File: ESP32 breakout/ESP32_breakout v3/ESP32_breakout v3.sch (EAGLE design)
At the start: 54 parts, among them J3 SCHA4B0419, Q3 BSS84, U1 ESP-WROOM-32, U2 NCP-1117223-3, U3 MCP2221ATSSOP14

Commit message: Layout and 80% routing done
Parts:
- removed R13: 10k, dr-library:RESISTOR0603
- added JP7, JP8: JUMPER_2-WAY, dr-library:JUMPER_2-WAY
- added R3: 10k, dr-library:RESISTOR0603
- renumbered S1 to RST, S2 to BOOT
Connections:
- new net N$1: JP7.1, R9.1
- new net N$6: JP8.1, R3.1
- net +3V3: now also JP7.2, JP8.2; no longer R13.1, R9.1
- net CLK: no longer J3.CLK, R12.2
- net CMD: no longer J3.CMD, R11.2
- net IO12/T5: now also J3.DAT2, R9.2
- net IO13/T4: now also J3.DAT3/CMD, R10.2
- net IO14/T6: now also J3.CLK, R12.2
- net IO15/T3: now also J3.CMD, R11.2
- net IO2/T2: now also J3.DAT0, R3.2
- net IO4/T0: now also J3.DAT1, R14.2
- net SD0: no longer J3.DAT0, R13.2
- net SD1: no longer J3.DAT1, R14.2
- net SD2: no longer J3.DAT2, R9.2
- net SD3: no longer J3.DAT3/CMD, R10.2
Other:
- moved on the sheet: C19, J3, R10, R11, R12, R14, R9

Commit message: v3 routing
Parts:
- added JP10, JP9: M02LONG, dr-library:M02LONG
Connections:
- net +3V3: now also JP10.2
- net GND: now also JP10.1, JP9.1
- net VCC: now also JP9.2
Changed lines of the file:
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@@
 <part name="+3V8" library="supply1" deviceset="+3V3" device=""/>
 <part name="+3V9" library="supply1" deviceset="+3V3" device=""/>
+<part name="P+2" library="supply1" deviceset="VCC" device=""/>
+<part name="+3V13" library="supply1" deviceset="+3V3" device=""/>
+<part name="GND7" library="supply1" deviceset="GND" device=""/>
+<part name="GND11" library="supply1" deviceset="GND" device=""/>
+<part name="JP9" library="dr-library" deviceset="M02" device="LONG"/>
+<part name="JP10" library="dr-library" deviceset="M02" device="LONG"/>
 </parts>
 <sheets>
@@
 <instance part="+3V8" gate="G$1" x="248.92" y="241.3"/>
 <instance part="+3V9" gate="G$1" x="248.92" y="223.52"/>
+<instance part="P+2" gate="VCC" x="106.68" y="220.98"/>
+<instance part="+3V13" gate="G$1" x="129.54" y="220.98"/>
+<instance part="GND7" gate="1" x="106.68" y="205.74"/>
+<instance part="GND11" gate="1" x="129.54" y="205.74"/>
+<instance part="JP9" gate="G$1" x="114.3" y="213.36" rot="R180"/>
+<instance part="JP10" gate="G$1" x="137.16" y="213.36" rot="R180"/>
 </instances>
 <busses>
@@
 <wire x1="198.12" y1="43.18" x2="200.66" y2="43.18" width="0.1524" layer="91"/>
 <junction x="200.66" y="43.18"/>
+</segment>
+<segment>
+<wire x1="132.08" y1="210.82" x2="129.54" y2="210.82" width="0.1524" layer="91"/>
+<pinref part="GND11" gate="1" pin="GND"/>
+<wire x1="129.54" y1="210.82" x2="129.54" y2="208.28" width="0.1524" layer="91"/>
+<pinref part="JP10" gate="G$1" pin="1"/>
+</segment>
+<segment>
+<wire x1="109.22" y1="210.82" x2="106.68" y2="210.82" width="0.1524" layer="91"/>
+<pinref part="GND7" gate="1" pin="GND"/>
+<wire x1="106.68" y1="210.82" x2="106.68" y2="208.28" width="0.1524" layer="91"/>
+<pinref part="JP9" gate="G$1" pin="1"/>
 </segment>
 </net>
@@
 <pinref part="+3V9" gate="G$1" pin="+3V3"/>
 </segment>
+<segment>
+<wire x1="132.08" y1="213.36" x2="129.54" y2="213.36" width="0.1524" layer="91"/>
+<pinref part="+3V13" gate="G$1" pin="+3V3"/>
+<wire x1="129.54" y1="213.36" x2="129.54" y2="218.44" width="0.1524" layer="91"/>
+<pinref part="JP10" gate="G$1" pin="2"/>
+</segment>
 </net>
 <net name="EN" class="0">
@@
 <pinref part="P+5" gate="VCC" pin="VCC"/>
 </segment>
+<segment>
+<wire x1="109.22" y1="213.36" x2="106.68" y2="213.36" width="0.1524" layer="91"/>
+<pinref part="P+2" gate="VCC" pin="VCC"/>
+<wire x1="106.68" y1="213.36" x2="106.68" y2="218.44" width="0.1524" layer="91"/>
+<pinref part="JP9" gate="G$1" pin="2"/>
+</segment>
 </net>

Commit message: PCB made
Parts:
- removed D7: (no value), dr-library:LED1206
- removed R16: 330, dr-library:RESISTOR0603
- added D1: VS-10BQ030-M3, dr-library:VS-10BQ030-M3
- added R13: 10k, dr-library:RESISTOR0603
- D2: value VS-10BQ030-M3 -> (none); device dr-library:VS-10BQ030-M3 -> dr-library:LED1206
- JP10, JP9: value M02LONG -> JUMPER_3-WAY; device dr-library:M02LONG -> dr-library:JUMPER_3-WAY
- JP6, JP7: value JUMPER_2-WAY -> M02LONG; device dr-library:JUMPER_2-WAY -> dr-library:M02LONG
- R9: value 10k -> 330
- renumbered C18 to C8, C19 to C9, RST to RESET
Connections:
- removed net N$1: JP7.1, R9.1
- new net N$7: JP10.1, R15.1
- net +3V3: now also JP9.2, R13.1; no longer JP8.2, R14.1
- net GND: now also D2.C, JP6.1, JP7.1; no longer D7.C, JP10.1, JP9.1
- net HEART: now also JP8.1; no longer JP6.1
- net IO12/T5: now also R14.2; no longer R9.2
- net IO19: now also JP8.2; no longer JP6.2
- net IO2/T2: now also R15.2; no longer R3.2
- net IO4/T0: now also R13.2; no longer R14.2
- net N$10: now also R9.2; no longer R7.2
- net N$11: now also D4.A; no longer D5.A
- net N$2: now also D1.A; no longer D2.A
- net N$3: now also R3.1; no longer R15.1
- net N$4: now also D5.A, R7.1; no longer D7.A, R16.1
- net N$5: now also D2.A; no longer D3.A
- net N$6: now also JP9.1, R14.1; no longer JP8.1, R3.1
- net N$8: now also D3.A; no longer D4.A
- net N$9: now also R9.1; no longer R7.1
- net USBCFG: now also R7.2; no longer R16.2
- net VCC: now also D1.C, JP6.2; no longer D2.C, JP9.2
- net V_MCP: now also R3.2; no longer R15.2
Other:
- moved on the sheet: D3, D4, D5, JP6, JP7, JP8, R14, R15, R3, R7, R9

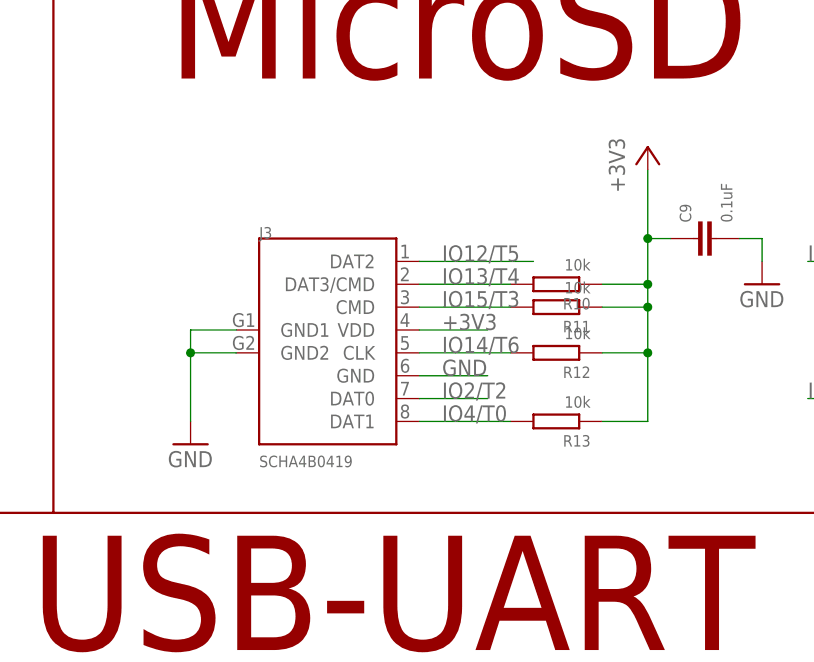
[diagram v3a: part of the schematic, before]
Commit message: Added LED for microSD CD
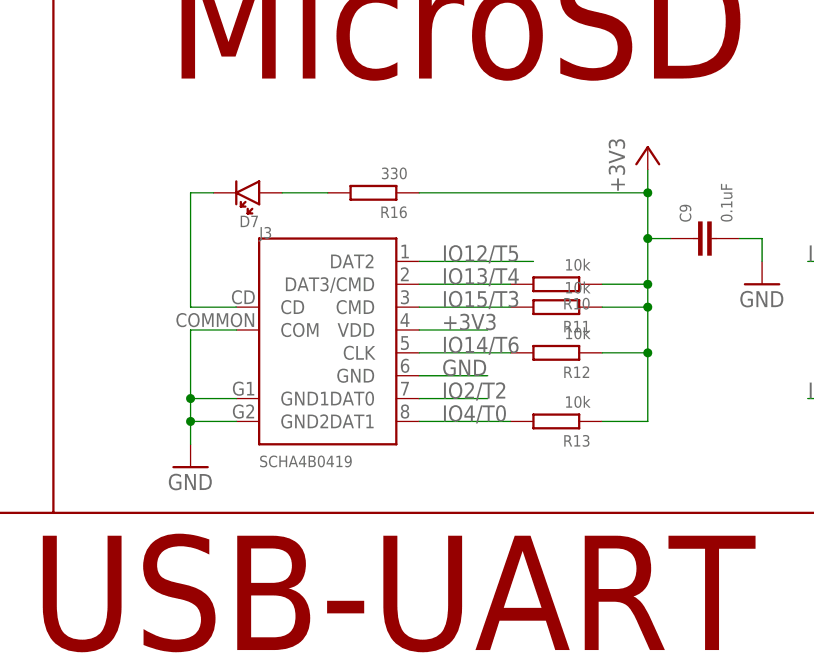
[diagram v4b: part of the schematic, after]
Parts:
- added D7: (no value), dr-library:LED1206
- added R16: 330, dr-library:RESISTOR0603
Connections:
- new net N$12: D7.C, J3.CD
- new net N$14: D7.A, R16.2
- net +3V3: now also R16.1
- net GND: now also J3.COM
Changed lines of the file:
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@@
 <part name="JP10" library="dr-library" deviceset="JUMPER_3-WAY" device=""/>
 <part name="+3V8" library="supply1" deviceset="+3V3" device=""/>
+<part name="R16" library="dr-library" deviceset="RESISTOR" device="0603" value="330"/>
+<part name="D7" library="dr-library" deviceset="LED" device="1206"/>
 </parts>
 <sheets>
@@
 <instance part="GND9" gate="1" x="160.02" y="129.54"/>
 <instance part="+3V5" gate="G$1" x="187.96" y="172.72"/>
-<instance part="GND12" gate="1" x="162.56" y="208.28"/>
+<instance part="GND12" gate="1" x="162.56" y="205.74"/>
 <instance part="U2" gate="G$1" x="71.12" y="228.6"/>
 <instance part="C5" gate="G$1" x="53.34" y="223.52"/>
@@
 <instance part="JP10" gate="G$1" x="256.54" y="218.44" rot="R180"/>
 <instance part="+3V8" gate="G$1" x="248.92" y="223.52"/>
+<instance part="R16" gate="G$1" x="182.88" y="236.22" rot="R180"/>
+<instance part="D7" gate="G$1" x="170.18" y="236.22" rot="R180"/>
 </instances>
 <busses>
@@
 </segment>
 <segment>
-<wire x1="167.64" y1="220.98" x2="162.56" y2="220.98" width="0.1524" layer="91"/>
+<wire x1="167.64" y1="213.36" x2="162.56" y2="213.36" width="0.1524" layer="91"/>
 <pinref part="GND12" gate="1" pin="GND"/>
-<wire x1="162.56" y1="220.98" x2="162.56" y2="218.44" width="0.1524" layer="91"/>
-<wire x1="162.56" y1="218.44" x2="162.56" y2="210.82" width="0.1524" layer="91"/>
-<wire x1="167.64" y1="218.44" x2="162.56" y2="218.44" width="0.1524" layer="91"/>
-<junction x="162.56" y="218.44"/>
+<wire x1="162.56" y1="213.36" x2="162.56" y2="210.82" width="0.1524" layer="91"/>
+<wire x1="162.56" y1="210.82" x2="162.56" y2="208.28" width="0.1524" layer="91"/>
+<wire x1="167.64" y1="210.82" x2="162.56" y2="210.82" width="0.1524" layer="91"/>
+<junction x="162.56" y="210.82"/>
 <pinref part="J3" gate="G$1" pin="GND1"/>
 <pinref part="J3" gate="G$1" pin="GND2"/>
+<pinref part="J3" gate="G$1" pin="COM"/>
+<wire x1="167.64" y1="220.98" x2="162.56" y2="220.98" width="0.1524" layer="91"/>
+<wire x1="162.56" y1="220.98" x2="162.56" y2="213.36" width="0.1524" layer="91"/>
+<junction x="162.56" y="213.36"/>
 </segment>
 <segment>
@@
 <pinref part="+3V12" gate="G$1" pin="+3V3"/>
 <pinref part="R13" gate="G$1" pin="1"/>
-<wire x1="213.36" y1="238.76" x2="213.36" y2="231.14" width="0.1524" layer="91"/>
+<wire x1="213.36" y1="238.76" x2="213.36" y2="236.22" width="0.1524" layer="91"/>
+<wire x1="213.36" y1="236.22" x2="213.36" y2="231.14" width="0.1524" layer="91"/>
 <wire x1="213.36" y1="231.14" x2="213.36" y2="226.06" width="0.1524" layer="91"/>
 <wire x1="213.36" y1="226.06" x2="213.36" y2="223.52" width="0.1524" layer="91"/>
@@
 <wire x1="215.9" y1="231.14" x2="213.36" y2="231.14" width="0.1524" layer="91"/>
 <junction x="213.36" y="231.14"/>
+<pinref part="R16" gate="G$1" pin="1"/>
+<wire x1="187.96" y1="236.22" x2="213.36" y2="236.22" width="0.1524" layer="91"/>
+<junction x="213.36" y="236.22"/>
 </segment>
 <segment>
@@
 </segment>
 </net>
+<net name="N$12" class="0">
+<segment>
+<pinref part="J3" gate="G$1" pin="CD"/>
+<wire x1="167.64" y1="223.52" x2="162.56" y2="223.52" width="0.1524" layer="91"/>
+<pinref part="D7" gate="G$1" pin="C"/>
+<wire x1="165.1" y1="236.22" x2="162.56" y2="236.22" width="0.1524" layer="91"/>
+<wire x1="162.56" y1="236.22" x2="162.56" y2="223.52" width="0.1524" layer="91"/>
+</segment>
+</net>
+<net name="N$14" class="0">
+<segment>
+<pinref part="R16" gate="G$1" pin="2"/>
+<pinref part="D7" gate="G$1" pin="A"/>
+<wire x1="177.8" y1="236.22" x2="172.72" y2="236.22" width="0.1524" layer="91"/>
+</segment>
+</net>
